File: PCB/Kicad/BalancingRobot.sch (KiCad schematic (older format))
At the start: 10 parts, among them P1 PWM, P2 BT_USB, P3 CONN_1, P4 CONN_1, P5 CONN_1, P6 CONN_1, U1 74HC00, U2 GY-521, U3 XL7105-SY

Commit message: primera version del PCB
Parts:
- removed P1: PWM, symbol CONN_5
- added C1, C3: 0.1u, ~, symbol C
- added C2, C4: 10u, ~, symbol CAPAPOL
- added D1: DIODE, ~, symbol DIODE
- added JP1: JUMPER, ~, symbol JUMPER
- added P1: PWM, symbol CONN_6
- added P7: CONN_2, symbol CONN_2
- added P8: PWR, symbol CONN_2
- added R1, R2, R3: R, ~, symbol R
- added U?1: MCP1700T-33, ~, symbol MCP1700T-33
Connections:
- net GIO: now also APM1.8 (5); no longer APM1.9 (6)
- net GND: now also C2.2, C3.2, C4.2, P1.6, P7.2 (PM), P8.2 (PM), R2.1, U?1.1 (GND)
- net PWM1A: now also P1.4
- net PWM1B: now also P1.5
- net PWM2A: now also P1.2
- net PWM2B: now also P1.3
- net RST: now also C1.1; no longer P2.1
- net SCK: now also APM1.6 (3); no longer APM1.8 (5)
- net SCS: now also APM1.5 (2); no longer APM1.6 (3)
- net VCC: now also C3.1, C4.1, D1.2 (K), JP1.2, U?1.3 (OUT)
- net BAT: now reaches APM1.19 (A2)
- net BAT: now also D1.1 (A), R1.1
- new net: P7.1 (P1), R3.2
- new net: C2.1, R1.2, R2.2, R3.1
- new net: JP1.1, P8.1 (P1), U?1.2 (IN)
- new net DTR: C1.2, P2.1
- new net EN_HB: APM1.9 (6), P1.1
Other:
- moved on the sheet: APM1, P2, P3, P4, P5, P6, U1A, U1B, U1C, U1D, U2, U3

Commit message: v1 del PCB y diagrama, primera version construida
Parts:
- removed P1: PWM, symbol CONN_6
- added P1: PWM, symbol CONN_8
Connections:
- net EN_HB: now also P1.2 (P2)
- net GND: now also P1.1 (P1), P1.8 (P8)
- net PWM1A: now also P1.5 (P5)
- net PWM1B: now also P1.6 (P6)
- net PWM2A: now also P1.3 (P3)
- net PWM2B: now also P1.4 (P4)
- net VCC: now also P1.7 (P7)
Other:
- note added: "PB0"
- note added: "PB1"
- note added: "PB2"
- note added: "PB3"
- note added: "PB4"
- note added: "PB5"
- note added: "PC0"
- note added: "PC1"
- note added: "PC2"
- note added: "PC3"
- note added: "PC4"
- note added: "PC5"
- note added: "PD2"
- note added: "PD3"
- note added: "PD4"
- note added: "PD5"
- note added: "PD6"
- note added: "PD7"
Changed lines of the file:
@@
 Sheet 1 1
 Title "Robot Balancista"
-Date "9 aug 2015"
+Date "12 aug 2015"
 Rev "1"
 Comp "Fabián Inostroza"
@@
 Text Label 9100 2650 0    60   ~ 0
 PWM2A
-Text Label 8900 3100 0    60   ~ 0
+Text Label 8850 3100 0    60   ~ 0
 PWM2B
 Text Label 8900 4000 0    60   ~ 0
@@
 	7350 4100 7600 4100
 Wire Wire Line
-	8800 2650 9250 2650
-Wire Wire Line
-	9250 2650 9250 3350
-Wire Wire Line
-	9250 3350 9450 3350
+	8800 2650 9200 2650
+Wire Wire Line
+	9200 2650 9200 3350
+Wire Wire Line
+	9200 3350 9450 3350
 Wire Wire Line
 	9450 3450 9050 3450
@@
 	9250 4450 8800 4450
 Wire Wire Line
-	9450 3750 9400 3750
-Wire Wire Line
-	9400 3750 9400 4150
+	8850 3750 9450 3750
 Wire Wire Line
 	5300 3250 5850 3250
@@
 Wire Wire Line
 	5500 3650 5300 3650
-$Comp
-L CONN_6 P1
-U 1 1 55C6864F
-P 9800 3500
-F 0 "P1" V 9750 3500 60  0000 C CNN
-F 1 "PWM" V 9850 3500 60  0000 C CNN
-F 2 "" H 9800 3500 60  0000 C CNN
-F 3 "" H 9800 3500 60  0000 C CNN
-	1    9800 3500
-	1    0    0    -1
-$EndComp
-Wire Wire Line
-	9450 3250 9350 3250
-Wire Wire Line
-	9350 3250 9350 3100
-Text Label 9350 3100 0    60   ~ 0
+Wire Wire Line
+	9450 3250 9300 3250
+Wire Wire Line
+	9300 3250 9300 3100
+Text Label 9300 3100 0    60   ~ 0
 EN_HB
 Wire Wire Line
@@
 Wire Wire Line
 	2550 1350 2700 1350
+Text Notes 4400 3550 0    40   ~ 0
+PD2
+Text Notes 4400 3650 0    40   ~ 0
+PD3
+Text Notes 4400 3750 0    40   ~ 0
+PD4
+Text Notes 4400 3850 0    40   ~ 0
+PD5
+Text Notes 4400 3950 0    40   ~ 0
+PD6
+Text Notes 4400 4050 0    40   ~ 0
+PD7
+Text Notes 4400 4150 0    40   ~ 0
+PB0
+Text Notes 4400 4250 0    40   ~ 0
+PB1
+Text Notes 4800 3550 2    40   ~ 0
+PC3
+Text Notes 4800 3650 2    40   ~ 0
+PC2
+Text Notes 4800 3750 2    40   ~ 0
+PC1
+Text Notes 4800 3850 2    40   ~ 0
+PC0
+Text Notes 4800 3950 2    40   ~ 0
+PB5
+Text Notes 4800 4050 2    40   ~ 0
+PB4
+Text Notes 4800 4150 2    40   ~ 0
+PB3
+Text Notes 4800 4250 2    40   ~ 0
+PB2
+Text Notes 4400 4350 2    40   ~ 0
+PC4
+Text Notes 4800 4350 0    40   ~ 0
+PC5
+$Comp
+L CONN_8 P1
+U 1 1 55CBC4C5
+P 9800 3500
+F 0 "P1" V 9750 3500 60  0000 C CNN
+F 1 "PWM" V 9850 3500 60  0000 C CNN
+F 2 "" H 9800 3500 60  0000 C CNN
+F 3 "" H 9800 3500 60  0000 C CNN
+	1    9800 3500
+	1    0    0    -1
+$EndComp
+Wire Wire Line
+	9450 3850 9400 3850
+Wire Wire Line
+	9400 3150 9400 4150
+$Comp
+L VCC #PWR?
+U 1 1 55CBC5E0
+P 8850 3650
+F 0 "#PWR?" H 8850 3750 30  0001 C CNN
+F 1 "VCC" H 8850 3750 30  0000 C CNN
+F 2 "" H 8850 3650 60  0000 C CNN
+F 3 "" H 8850 3650 60  0000 C CNN
+	1    8850 3650
+	1    0    0    -1
+$EndComp
+Wire Wire Line
+	8850 3750 8850 3650
+Wire Wire Line
+	9450 3150 9400 3150
+Connection ~ 9400 3850
 $EndSCHEMATC

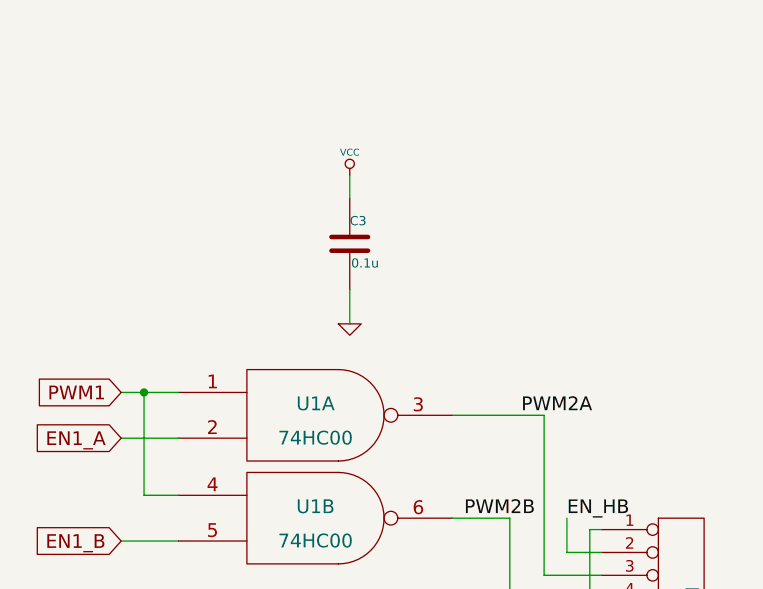
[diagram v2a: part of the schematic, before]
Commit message: Se agregaron resistencias pulldown en las señales PWM para que no se active el driver mientras el micro se esta iniciando
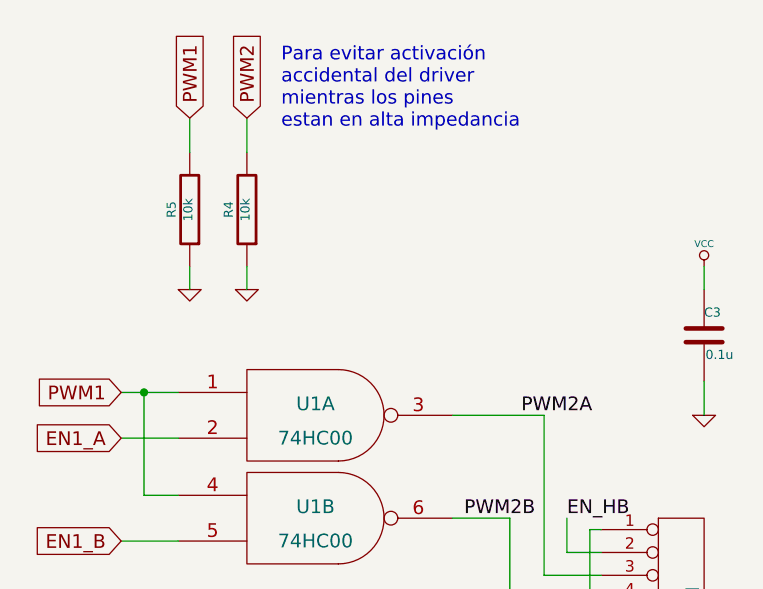
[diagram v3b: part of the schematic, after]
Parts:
- added R4, R5: 10k, ~, symbol R
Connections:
- net GND: now also R4.1, R5.1
- net PWM1: now also R5.2
- net PWM2: now also R4.2
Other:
- note added: "Para evitar activación \naccidental del driver\nmientras los pines \nestan en alta impedancia"
- moved on the sheet: C3
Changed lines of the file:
@@
 Sheet 1 1
 Title "Robot Balancista"
-Date "12 aug 2015"
+Date "17 aug 2015"
 Rev "1"
 Comp "Fabián Inostroza"
@@
 L C C3
 U 1 1 55C68DC7
-P 8350 1900
-F 0 "C3" H 8350 2000 40  0000 L CNN
-F 1 "0.1u" H 8356 1815 40  0000 L CNN
-F 2 "~" H 8388 1750 30  0000 C CNN
-F 3 "~" H 8350 1900 60  0000 C CNN
-	1    8350 1900
+P 9900 2300
+F 0 "C3" H 9900 2400 40  0000 L CNN
+F 1 "0.1u" H 9906 2215 40  0000 L CNN
+F 2 "~" H 9938 2150 30  0000 C CNN
+F 3 "~" H 9900 2300 60  0000 C CNN
+	1    9900 2300
 	1    0    0    -1
 $EndComp
@@
 L GND #PWR017
 U 1 1 55C68DCD
-P 8350 2250
-F 0 "#PWR017" H 8350 2250 30  0001 C CNN
-F 1 "GND" H 8350 2180 30  0001 C CNN
-F 2 "" H 8350 2250 60  0000 C CNN
-F 3 "" H 8350 2250 60  0000 C CNN
-	1    8350 2250
-	1    0    0    -1
-$EndComp
-Wire Wire Line
-	8350 2250 8350 2100
+P 9900 2650
+F 0 "#PWR017" H 9900 2650 30  0001 C CNN
+F 1 "GND" H 9900 2580 30  0001 C CNN
+F 2 "" H 9900 2650 60  0000 C CNN
+F 3 "" H 9900 2650 60  0000 C CNN
+	1    9900 2650
+	1    0    0    -1
+$EndComp
+Wire Wire Line
+	9900 2650 9900 2500
 $Comp
 L VCC #PWR018
 U 1 1 55C68E39
-P 8350 1600
-F 0 "#PWR018" H 8350 1700 30  0001 C CNN
-F 1 "VCC" H 8350 1700 30  0000 C CNN
-F 2 "" H 8350 1600 60  0000 C CNN
-F 3 "" H 8350 1600 60  0000 C CNN
-	1    8350 1600
-	1    0    0    -1
-$EndComp
-Wire Wire Line
-	8350 1600 8350 1700
+P 9900 2000
+F 0 "#PWR018" H 9900 2100 30  0001 C CNN
+F 1 "VCC" H 9900 2100 30  0000 C CNN
+F 2 "" H 9900 2000 60  0000 C CNN
+F 3 "" H 9900 2000 60  0000 C CNN
+	1    9900 2000
+	1    0    0    -1
+$EndComp
+Wire Wire Line
+	9900 2000 9900 2100
 $Comp
 L CONN_2 P8
@@
 	9400 3150 9400 4150
 $Comp
-L VCC #PWR?
+L VCC #PWR023
 U 1 1 55CBC5E0
 P 8850 3650
-F 0 "#PWR?" H 8850 3750 30  0001 C CNN
+F 0 "#PWR023" H 8850 3750 30  0001 C CNN
 F 1 "VCC" H 8850 3750 30  0000 C CNN
 F 2 "" H 8850 3650 60  0000 C CNN
@@
 	9450 3150 9400 3150
 Connection ~ 9400 3850
+Text GLabel 7900 1350 1    60   Input ~ 0
+PWM2
+Text GLabel 7650 1350 1    60   Input ~ 0
+PWM1
+$Comp
+L R R4
+U 1 1 55D1357B
+P 7900 1750
+F 0 "R4" V 7980 1750 40  0000 C CNN
+F 1 "10k" V 7907 1751 40  0000 C CNN
+F 2 "~" V 7830 1750 30  0000 C CNN
+F 3 "~" H 7900 1750 30  0000 C CNN
+	1    7900 1750
+	-1   0    0    1
+$EndComp
+$Comp
+L R R5
+U 1 1 55D13581
+P 7650 1750
+F 0 "R5" V 7730 1750 40  0000 C CNN
+F 1 "10k" V 7657 1751 40  0000 C CNN
+F 2 "~" V 7580 1750 30  0000 C CNN
+F 3 "~" H 7650 1750 30  0000 C CNN
+	1    7650 1750
+	-1   0    0    1
+$EndComp
+Wire Wire Line
+	7900 1350 7900 1500
+Wire Wire Line
+	7650 1350 7650 1500
+$Comp
+L GND #PWR024
+U 1 1 55D13707
+P 7900 2100
+F 0 "#PWR024" H 7900 2100 30  0001 C CNN
+F 1 "GND" H 7900 2030 30  0001 C CNN
+F 2 "" H 7900 2100 60  0000 C CNN
+F 3 "" H 7900 2100 60  0000 C CNN
+	1    7900 2100
+	1    0    0    -1
+$EndComp
+$Comp
+L GND #PWR025
+U 1 1 55D1370D
+P 7650 2100
+F 0 "#PWR025" H 7650 2100 30  0001 C CNN
+F 1 "GND" H 7650 2030 30  0001 C CNN
+F 2 "" H 7650 2100 60  0000 C CNN
+F 3 "" H 7650 2100 60  0000 C CNN
+	1    7650 2100
+	1    0    0    -1
+$EndComp
+Wire Wire Line
+	7650 2100 7650 2000
+Wire Wire Line
+	7900 2000 7900 2100
+Text Notes 8050 1400 0    60   ~ 0
+Para evitar activación \naccidental del driver\nmientras los pines \nestan en alta impedancia
 $EndSCHEMATC
